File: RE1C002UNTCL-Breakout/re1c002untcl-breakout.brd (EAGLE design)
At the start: 12.7 x 8.8 mm, 2 parts

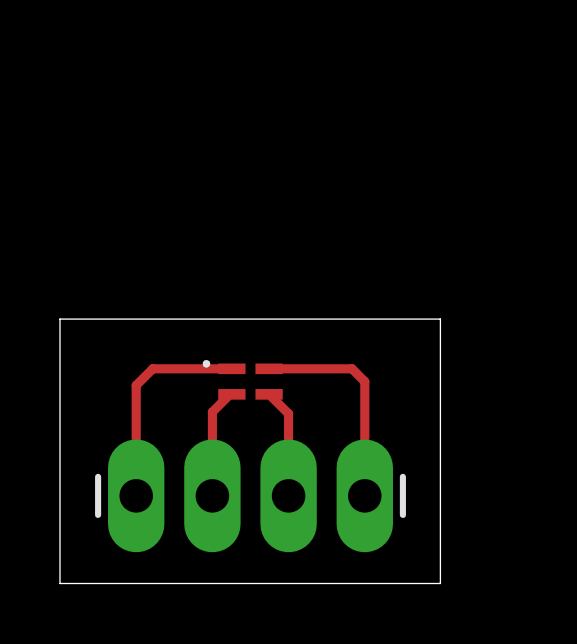
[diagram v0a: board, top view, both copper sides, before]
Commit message: new breakout
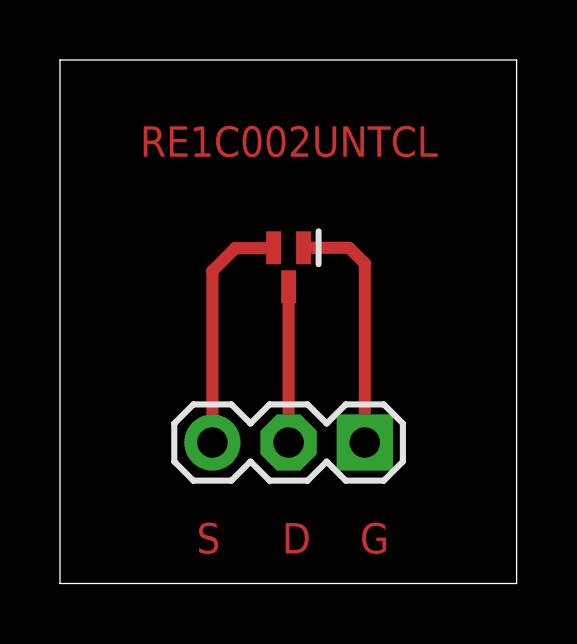
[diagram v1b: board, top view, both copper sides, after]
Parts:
- removed J1: (no value), connector:1X04_LONGPADS
- added IC1: RE1C002UNTCL, transitors:SOT50P160X85-3N
- U$1: value XZCMEDGCBD110W-RGB -> (none); device leds:1.6X1.6-RGB -> connector:1X03_UDPI
- moved U$1 4.32 mm to (10.2, 4.70)
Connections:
- removed net BLUE: J1.2, U$1.4
- removed net GREEN: J1.3, U$1.3
- removed net RED: J1.4, U$1.2
- removed net VCC: J1.1, U$1.1
- new net DRAIN: IC1.3, U$1.2
- new net GATE: IC1.1, U$1.1
- new net SRC: IC1.2, U$1.3
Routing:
- net GATE: track 0.00 -> 8.23 mm
- net SRC: track 0.00 -> 8.08 mm
- net RED: track 7.18 -> 0.00 mm
- net VCC: track 7.10 -> 0.00 mm
- net DRAIN: track 0.00 -> 5.19 mm
- net BLUE: track 3.69 -> 0.00 mm
- net GREEN: track 3.65 -> 0.00 mm
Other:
- board size 12.7 x 8.8 mm -> 15.2 x 17.4 mm
- board text added: "D"
- board text added: "G"
- board text added: "RE1C002UNTCL"
- board text added: "S"
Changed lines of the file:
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@@
 <?xml version="1.0" encoding="utf-8"?>
 <!DOCTYPE eagle SYSTEM "eagle.dtd">
-<eagle version="9.6.1">
+<eagle version="9.6.2">
 <drawing>
 <settings>
@@
 <setting verticaltext="up"/>
 </settings>
-<grid distance="50" unitdist="mil" unit="mm" style="lines" multiple="1" display="yes" altdistance="5" altunitdist="mil" altunit="mm"/>
+<grid distance="50" unitdist="mil" unit="mm" style="lines" multiple="1" display="no" altdistance="5" altunitdist="mil" altunit="mm"/>
 <layers>
 <layer number="1" name="Top" color="4" fill="1" visible="yes" active="yes"/>
@@
 <board>
 <plain>
-<wire x1="0" y1="0" x2="12.68" y2="0" width="0" layer="20"/>
-<wire x1="12.68" y1="0" x2="12.68" y2="8.814" width="0" layer="20"/>
-<wire x1="12.68" y1="8.814" x2="0" y2="8.814" width="0" layer="20"/>
-<wire x1="0" y1="8.814" x2="0" y2="0" width="0" layer="20"/>
+<wire x1="0" y1="0" x2="15.22" y2="0" width="0" layer="20"/>
+<wire x1="15.22" y1="0" x2="15.22" y2="17.45" width="0" layer="20"/>
+<wire x1="15.22" y1="17.45" x2="0" y2="17.45" width="0" layer="20"/>
+<wire x1="0" y1="17.45" x2="0" y2="0" width="0" layer="20"/>
+<text x="2.667" y="14.224" size="1.016" layer="1">RE1C002UNTCL</text>
+<text x="4.55" y="1" size="1.016" layer="1">S</text>
+<text x="7.4" y="1" size="1.016" layer="1">D</text>
+<text x="10" y="1" size="1.016" layer="1">G</text>
 </plain>
 <attributes>
@@
 </autorouter>
 <elements>
-<element name="J1" library="connector" package="1X04_LONGPADS" value="" x="2.54" y="2.921" smashed="yes">
-<attribute name="PROD_ID" value="CONN-09696" x="25.4" y="-7.239" size="1.778" layer="27" display="off"/>
-<attribute name="VALUE" x="1.27" y="-0.889" size="1.27" layer="27"/>
+<element name="IC1" library="transitors" package="SOT50P160X85-3N" value="RE1C002UNTCL" x="7.62" y="10.541" smashed="yes" rot="R270">
+<attribute name="DESCRIPTION" value="MOSFET 1.2V Drive Nch MOSFET" x="0" y="-9.779" size="1.778" layer="27" rot="R270" display="off"/>
+<attribute name="HEIGHT" value="0.85mm" x="0" y="-9.779" size="1.778" layer="27" rot="R270" display="off"/>
+<attribute name="MANUFACTURER_NAME" value="ROHM Semiconductor" x="0" y="-9.779" size="1.778" layer="27" rot="R270" display="off"/>
+<attribute name="MANUFACTURER_PART_NUMBER" value="RE1C002UNTCL" x="0" y="-9.779" size="1.778" layer="27" rot="R270" display="off"/>
+<attribute name="MOUSER_PART_NUMBER" value="755-RE1C002UNTCL" x="0" y="-9.779" size="1.778" layer="27" rot="R270" display="off"/>
+<attribute name="MOUSER_PRICE-STOCK" value="https://www.mouser.com/Search/Refine.aspx?Keyword=755-RE1C002UNTCL" x="0" y="-9.779" size="1.778" layer="27" rot="R270" display="off"/>
 </element>
-<element name="U$1" library="leds" package="1.6X1.6-RGB" value="XZCMEDGCBD110W-RGB" x="6.35" y="6.731" smashed="yes" rot="R180"/>
+<element name="U$1" library="connector" package="1X03_UDPI" value="" x="10.16" y="4.699" smashed="yes" rot="R180">
+<attribute name="VALUE" x="11.43" y="7.874" size="1.27" layer="27" rot="R180"/>
+</element>
 </elements>
 <signals>
-<signal name="VCC">
+<signal name="GATE">
+<contactref element="IC1" pad="1"/>
 <contactref element="U$1" pad="1"/>
-<contactref element="J1" pad="1"/>
-<wire x1="5.7299" y1="7.156" x2="3.092" y2="7.156" width="0.3048" layer="1"/>
-<wire x1="3.092" y1="7.156" x2="2.54" y2="6.604" width="0.3048" layer="1"/>
-<wire x1="2.54" y1="6.604" x2="2.54" y2="2.921" width="0.3048" layer="1"/>
+<wire x1="8.12" y1="11.191" x2="9.637" y2="11.191" width="0.4064" layer="1"/>
+<wire x1="9.637" y1="11.191" x2="10.16" y2="10.668" width="0.4064" layer="1"/>
+<wire x1="10.16" y1="10.668" x2="10.16" y2="4.699" width="0.4064" layer="1"/>
 </signal>
-<signal name="GREEN">
-<contactref element="J1" pad="3"/>
+<signal name="SRC">
+<contactref element="IC1" pad="2"/>
 <contactref element="U$1" pad="3"/>
-<wire x1="6.9701" y1="6.306" x2="7.62" y2="5.6561" width="0.3048" layer="1"/>
-<wire x1="7.62" y1="5.6561" x2="7.62" y2="2.921" width="0.3048" layer="1"/>
+<wire x1="7.12" y1="11.191" x2="7.105" y2="11.176" width="0.4064" layer="1"/>
+<wire x1="7.105" y1="11.176" x2="5.842" y2="11.176" width="0.4064" layer="1"/>
+<wire x1="5.842" y1="11.176" x2="5.08" y2="10.414" width="0.4064" layer="1"/>
+<wire x1="5.08" y1="10.414" x2="5.08" y2="4.699" width="0.4064" layer="1"/>
 </signal>
-<signal name="BLUE">
-<contactref element="U$1" pad="4"/>
-<contactref element="J1" pad="2"/>
-<wire x1="5.7299" y1="6.306" x2="5.671" y2="6.306" width="0.3048" layer="1"/>
-<wire x1="5.671" y1="6.306" x2="5.08" y2="5.715" width="0.3048" layer="1"/>
-<wire x1="5.08" y1="5.715" x2="5.08" y2="2.921" width="0.3048" layer="1"/>
-</signal>
-<signal name="RED">
+<signal name="DRAIN">
+<contactref element="IC1" pad="3"/>
 <contactref element="U$1" pad="2"/>
-<contactref element="J1" pad="4"/>
-<wire x1="6.9701" y1="7.156" x2="9.735" y2="7.156" width="0.3048" layer="1"/>
-<wire x1="9.735" y1="7.156" x2="10.16" y2="6.731" width="0.3048" layer="1"/>
-<wire x1="10.16" y1="6.731" x2="10.16" y2="2.921" width="0.3048" layer="1"/>
+<wire x1="7.62" y1="4.699" x2="7.62" y2="9.891" width="0.4064" layer="1"/>
 </signal>
 </signals>
